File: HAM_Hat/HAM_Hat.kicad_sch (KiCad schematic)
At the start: 50 parts, among them J101 TL212V-02P-G12S, J102 DB-9RS-C, J103 NCW254-02S, J104 SMA6252A2, J105 NCW200S-04R, J3 FHDH2.54-40, M101 Fan, Q101 BSS138, Q102 BSS138, Q103 BSS138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

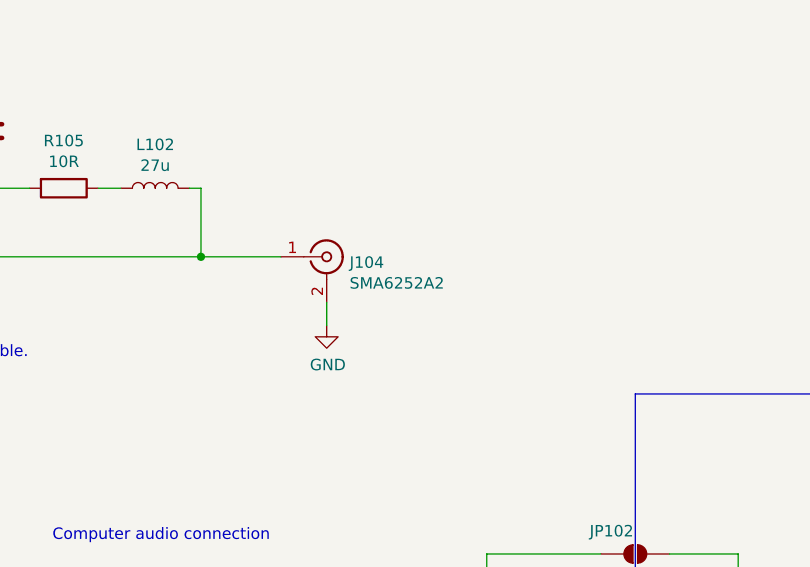
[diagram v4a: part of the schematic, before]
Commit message: Add u.fl connector instead of the SMA
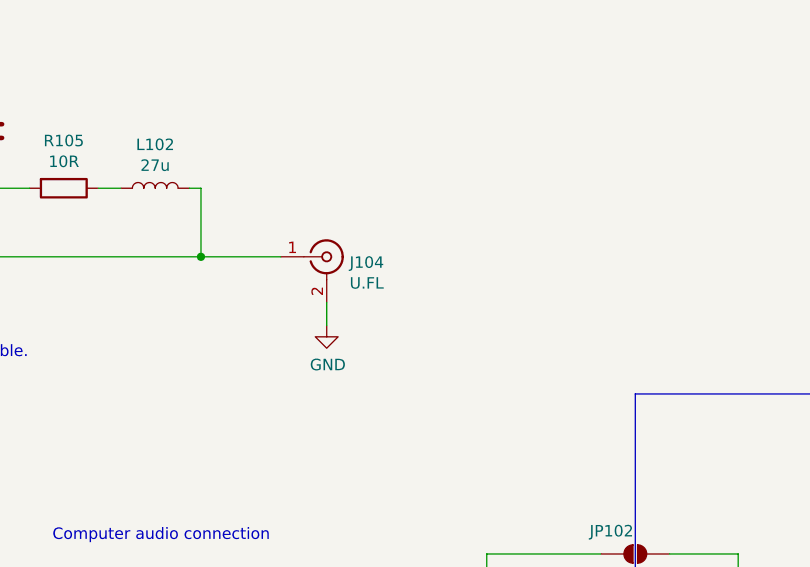
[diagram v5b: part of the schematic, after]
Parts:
- J104: value SMA6252A2 -> U.FL; id (none) -> 806
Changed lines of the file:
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@@
 			)
 		)
-		(property "Value" "SMA6252A2"
+		(property "Value" "U.FL"
 			(at 279.4 63.9064 0)
 			(effects
@@
 			)
 		)
-		(property "id" ""
+		(property "id" "806"
 			(at 276.86 60.96 0)
 			(effects

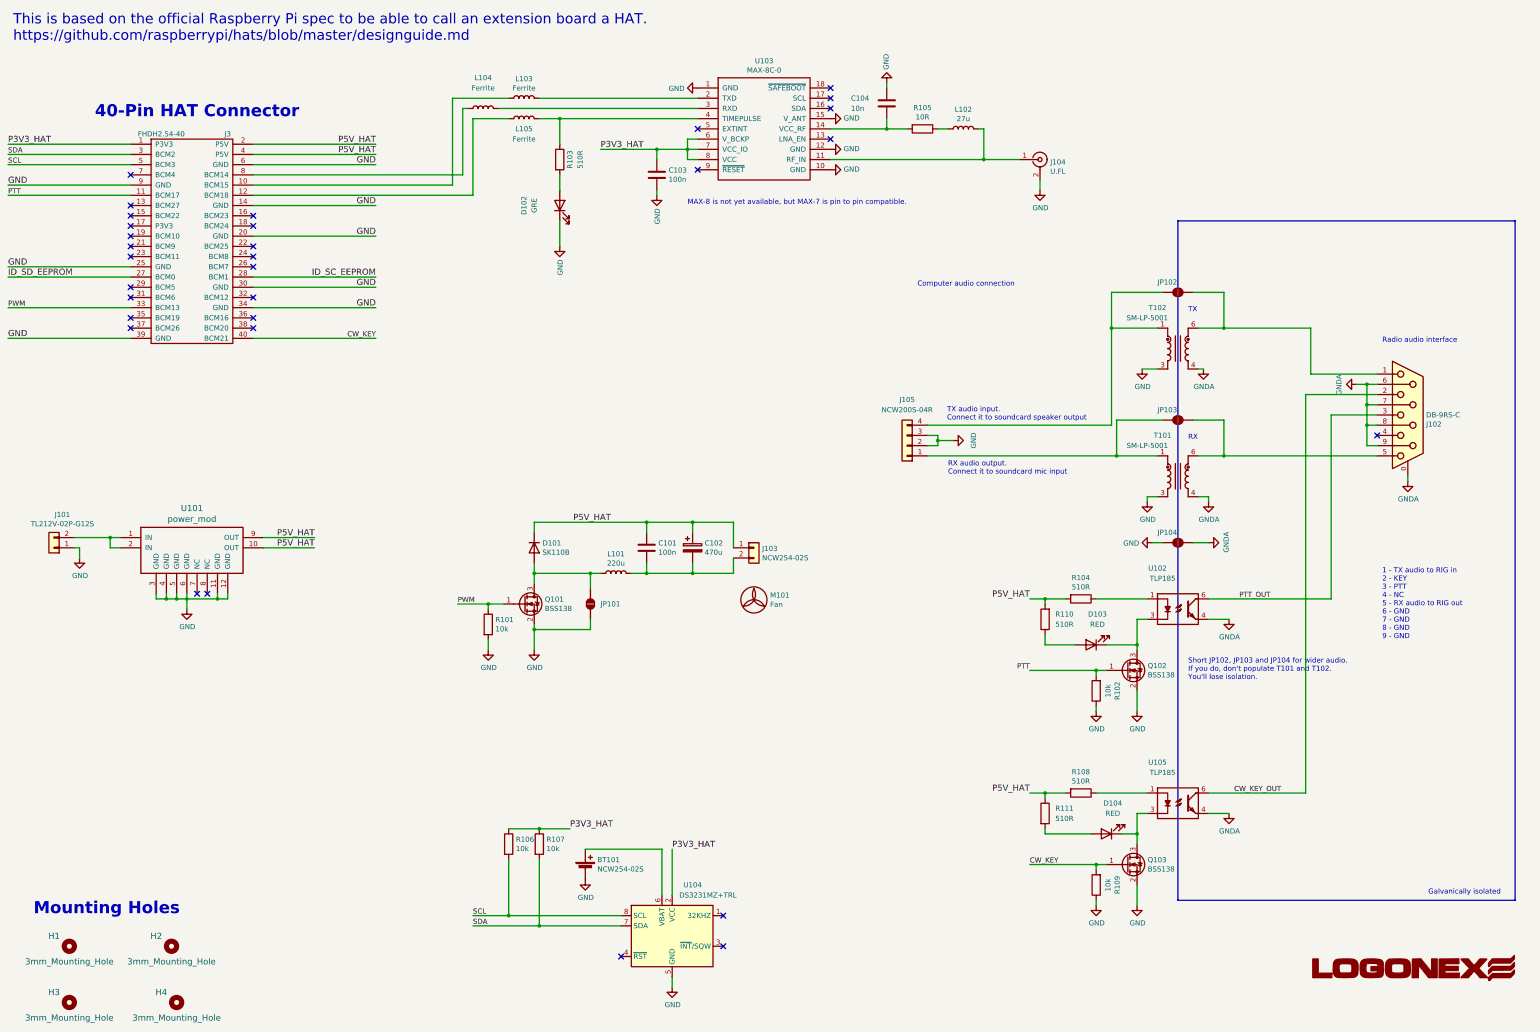
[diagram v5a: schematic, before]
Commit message: Add power LED
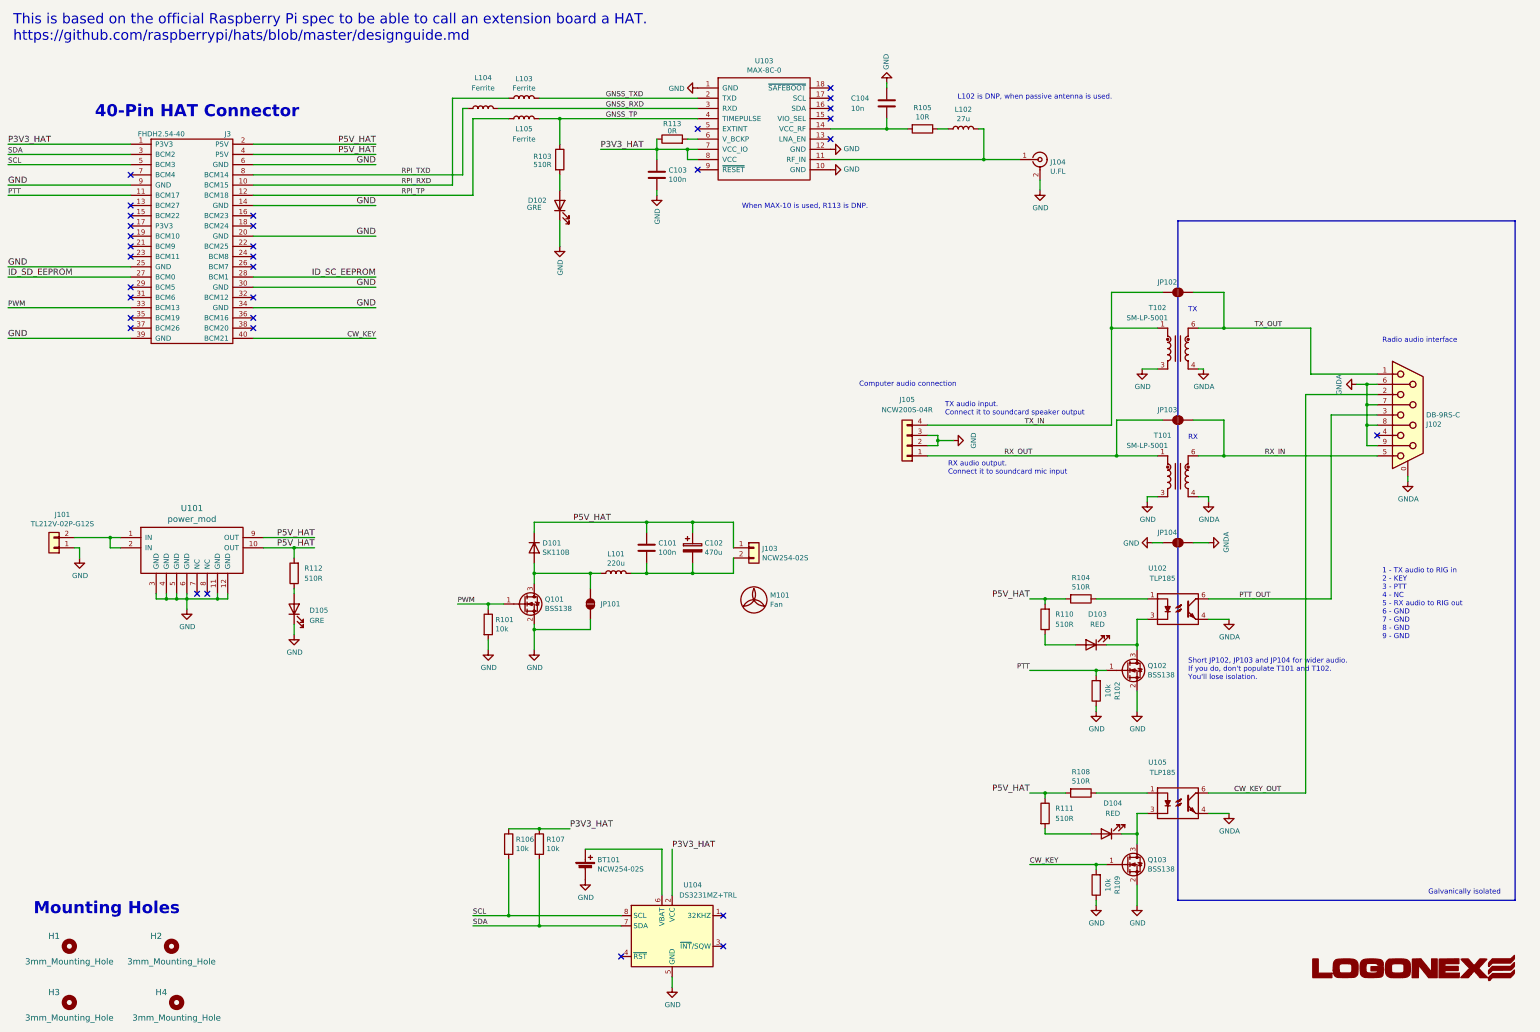
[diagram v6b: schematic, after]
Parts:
- added D105: GRE, LED_SMD:LED_0603_1608Metric, symbol default:levcsi_database/147
- added R112: 510R, Resistor_SMD:R_0603_1608Metric, symbol default:levcsi_database/390
- added R113: 0R, Resistor_SMD:R_0603_1608Metric, symbol default:levcsi_database/187
- J104: footprint Connector_Coaxial:U.FL_Molex_MCRF_73412-0110_Vertical -> l_connector:U.FL
- T101, T102: footprint Transformer_SMD:Pulse_PA2006NL -> l_transformer:SM_LP_5001
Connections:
- net GND: now also D105.1 (K); no longer U103.15 (V_ANT)
- net P3V3_HAT: now also R113.1; no longer U103.6 (V_BCKP)
- net P5V_HAT: now also R112.2
- net RPI_RXD: now reaches J3.10 (BCM15), L103.1
- net RPI_TP: now reaches J3.12 (BCM18), L105.1
- net RPI_TXD: now reaches J3.8 (BCM14), L104.1
- net TX_OUT: now reaches J102.1, JP102.2 (B), T102.6
- net RX_IN: now reaches J102.5, JP103.2 (B), T101.6
- net RX_OUT: now reaches J105.1 (Pin_1), JP103.1 (A), T101.1
- net TX_IN: now reaches J105.4 (Pin_4), JP102.1 (A), T102.1
- net GNSS_TXD: now reaches L103.2, U103.2 (TXD)
- net GNSS_RXD: now reaches L104.2, U103.3 (RXD)
- net GNSS_TP: now reaches L105.2, R103.1, U103.4 (TIMEPULSE)
- new net: R113.2, U103.6 (V_BCKP)
- new net: D105.2 (A), R112.1
- no-connect marks 31 -> 32
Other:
- note added: "L102 is DNP, when passive antenna is used."
- note added: "When MAX-10 is used, R113 is DNP."
- note removed: "MAX-8 is not yet available, but MAX-7 is pin to pin compatible."

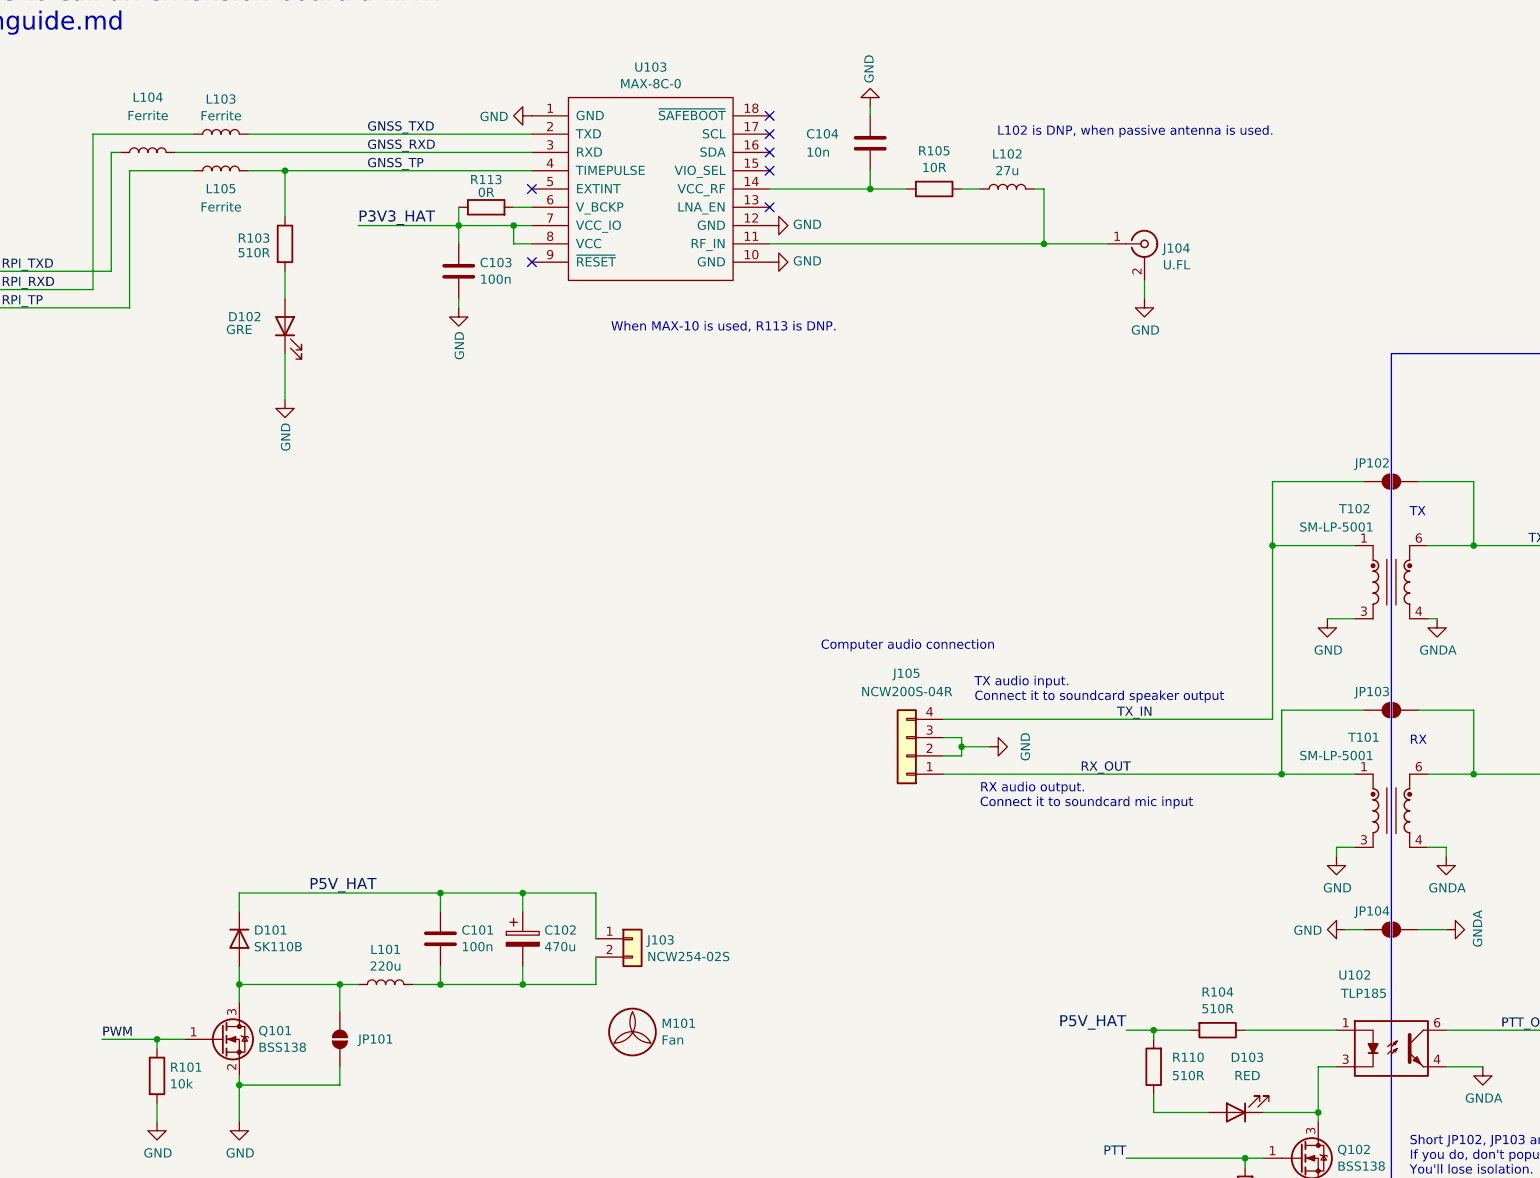
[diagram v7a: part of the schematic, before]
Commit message: U.FL connector replace
Migration to Kicad v9
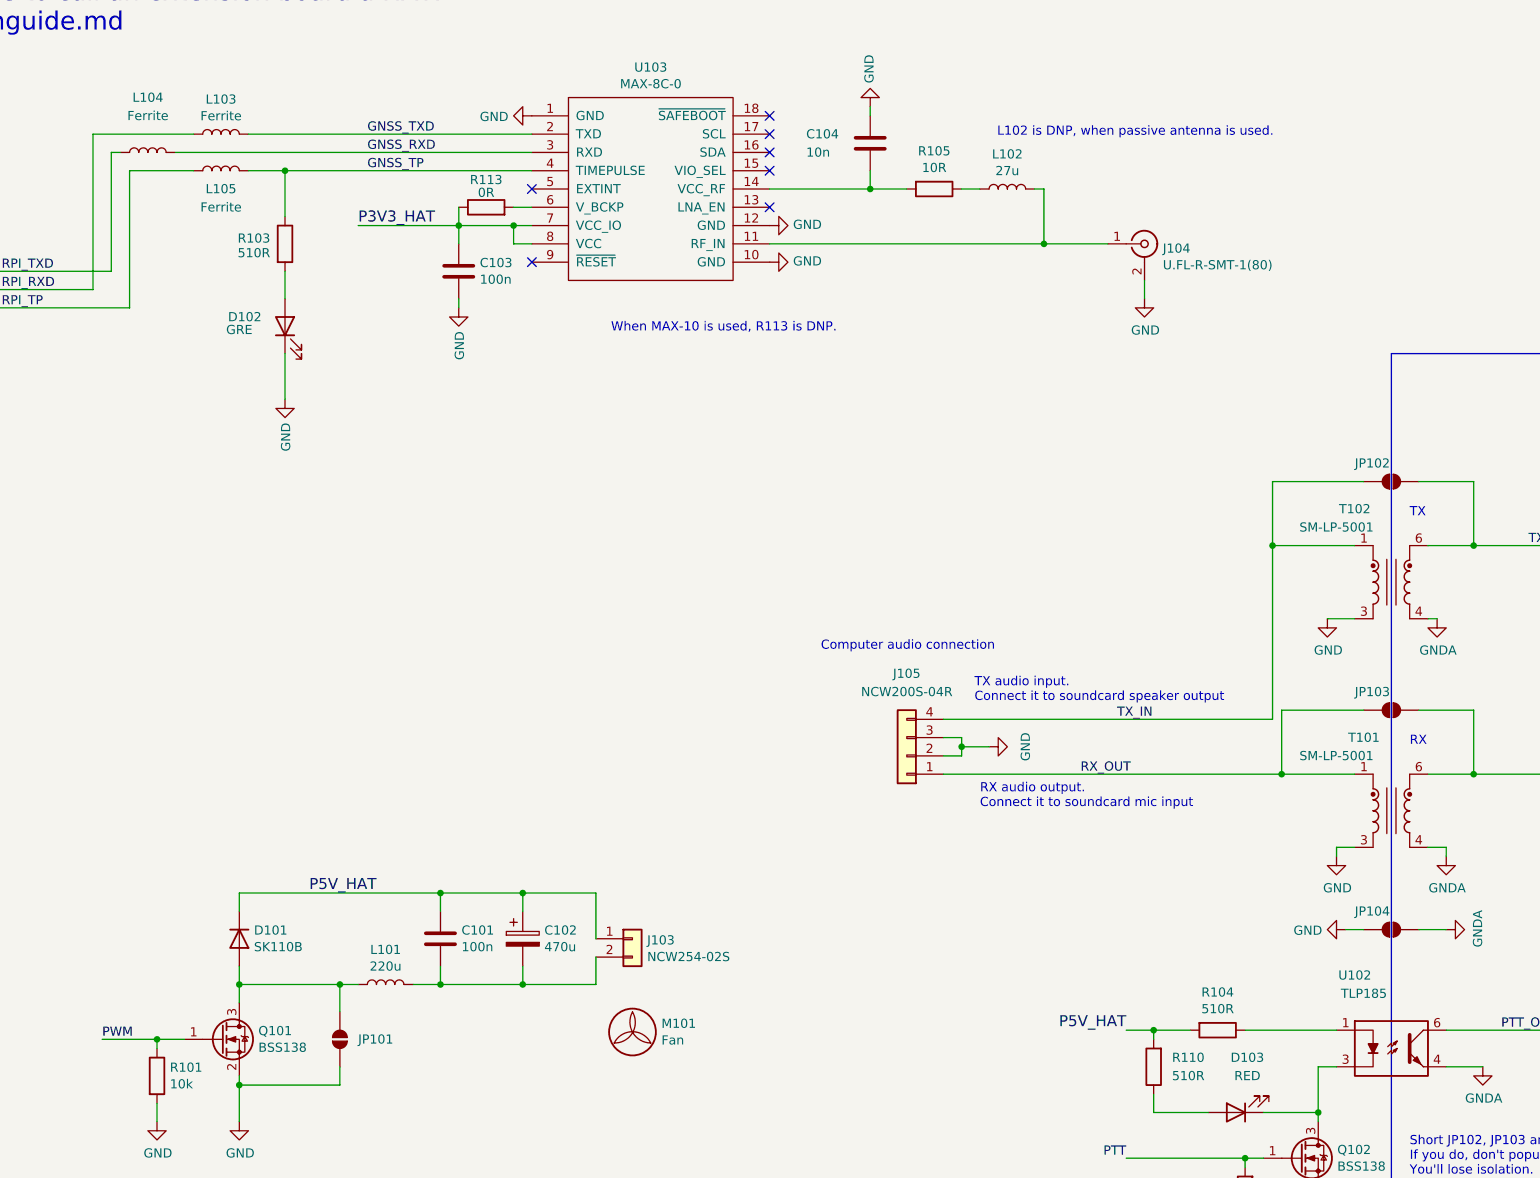
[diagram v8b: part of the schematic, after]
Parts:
- J104: value U.FL -> U.FL-R-SMT-1(80); footprint l_connector:U.FL -> Connector_Coaxial:U.FL_Hirose_U.FL-R-SMT-1_Vertical
